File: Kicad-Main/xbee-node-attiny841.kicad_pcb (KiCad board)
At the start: 2 copper layers, 58.5 x 58.5 mm, 40 parts, among them P10 CONN_1, P11 CONN_1, P12 CONN_1, P13 CONN_1, P14 CONN_1, P15 CONN_1, P16 CONN_1, P17 CONN_1, P18 CONN_1, P19 CONN_1, P2 XBee Adaptor, P20 CONN_1, P3 Debug Adaptor, P7 CONN_1, P8 CONN_1, P9 CONN_1, Q2 MMBT3904, Q3 2N7002, U1 ATTINY841, U2 MAX952ESA, U3 TPS77033

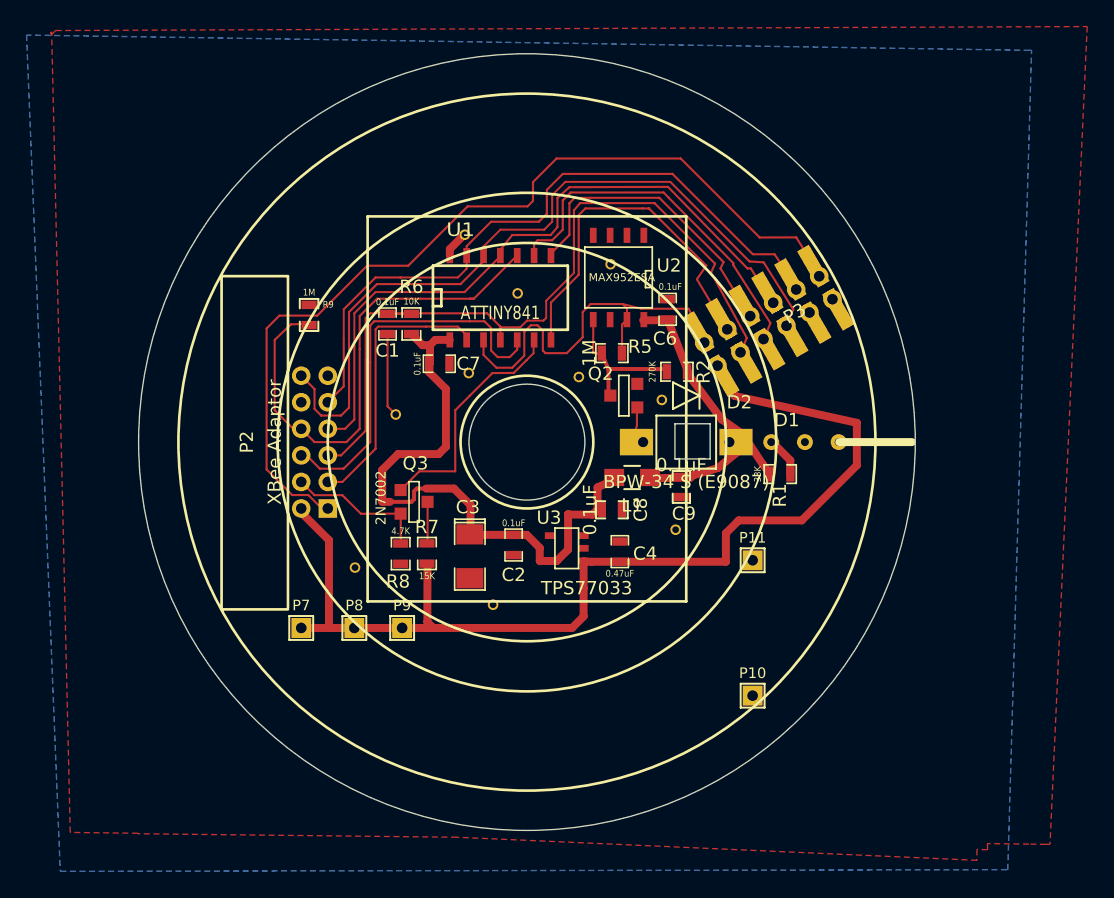
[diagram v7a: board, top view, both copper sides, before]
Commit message: Minor changes to PCB of main board
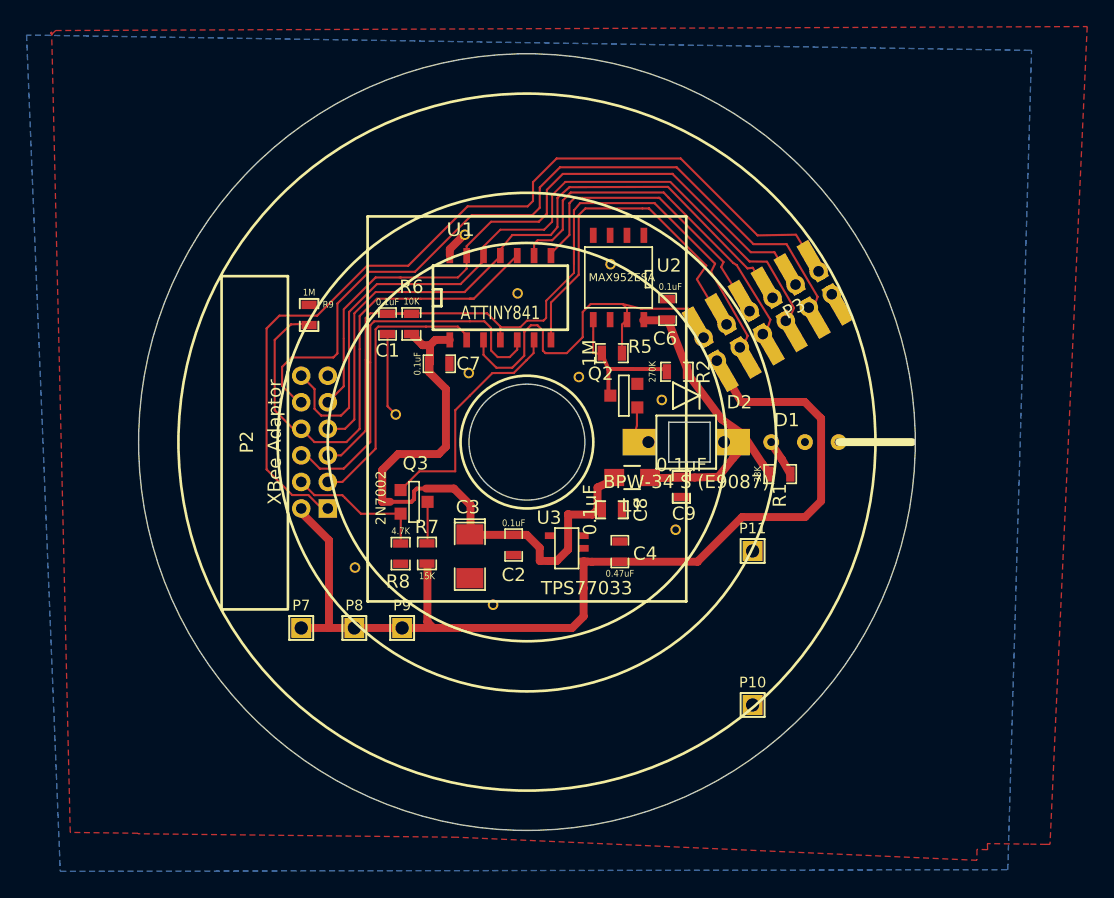
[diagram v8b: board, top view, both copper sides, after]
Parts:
- moved P10 0.70 mm to (217.0, 119.8)
- moved P11 0.70 mm to (217.0, 108.2)
- moved P3 0.38 mm to (219.0, 90.0)
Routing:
- net /Association: track 0.20 -> 59.0 mm
- net /Battery: track 84.3 -> 79.9 mm
- net /Commissioning: track 66.7 -> 68.7 mm
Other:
- outline, holes or cut-outs redrawn
